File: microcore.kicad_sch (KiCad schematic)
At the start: 7 parts, among them J1 TE_776231-1, J8 USB_B_Mini, M1 Module:mega-mcu100/0.3, M2 Module-power_12and5V-0.3, M3 Module-vr-max9924-0.3

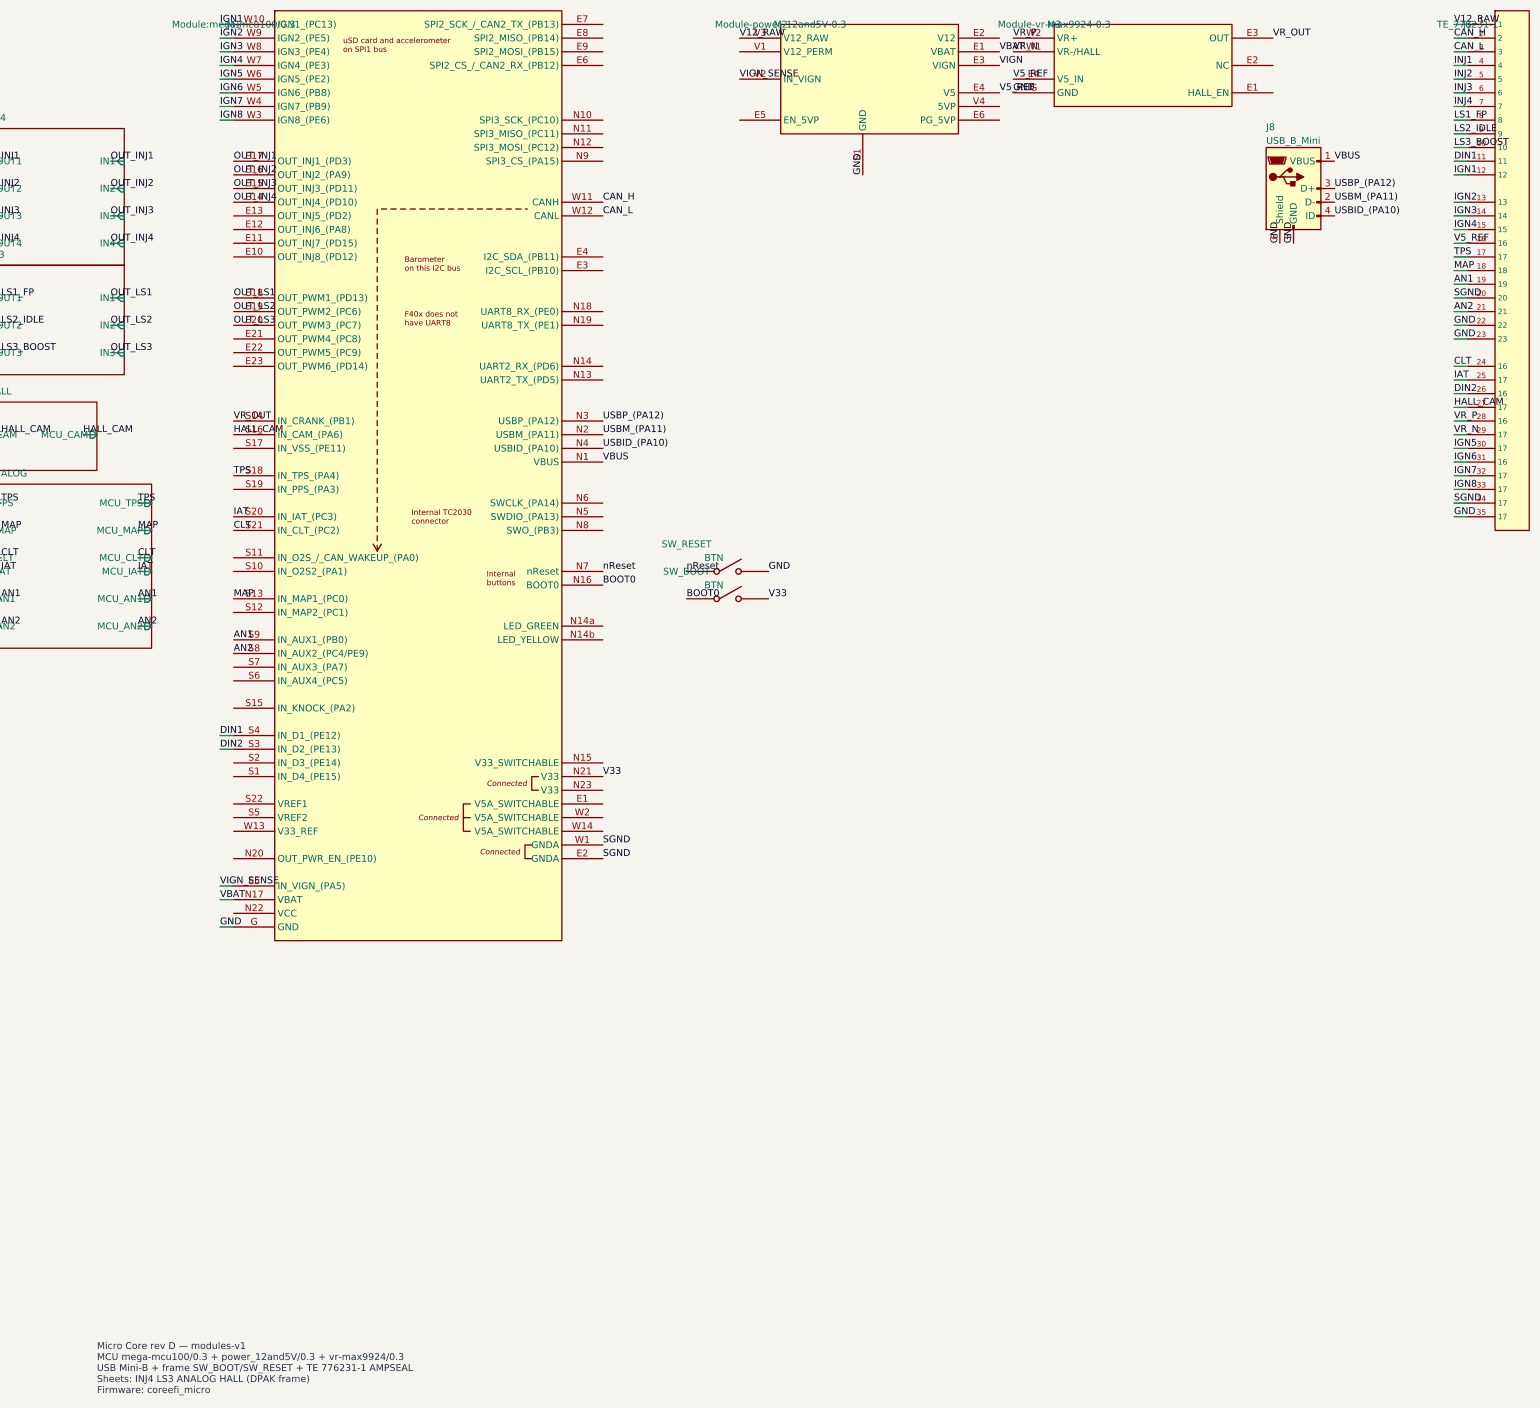
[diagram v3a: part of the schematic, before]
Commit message: Rev e: nest INJ/LS DPAKs on frame, apply netlist, GND pours, route
Place Q1-Q7 + R1-R7 clear of AMPSEAL keepout; unify GND global net;
assign schematic nets to pads; add F/B GND zones and scripted frame
tracks/vias. Module copper remains Create Board gerber merge.
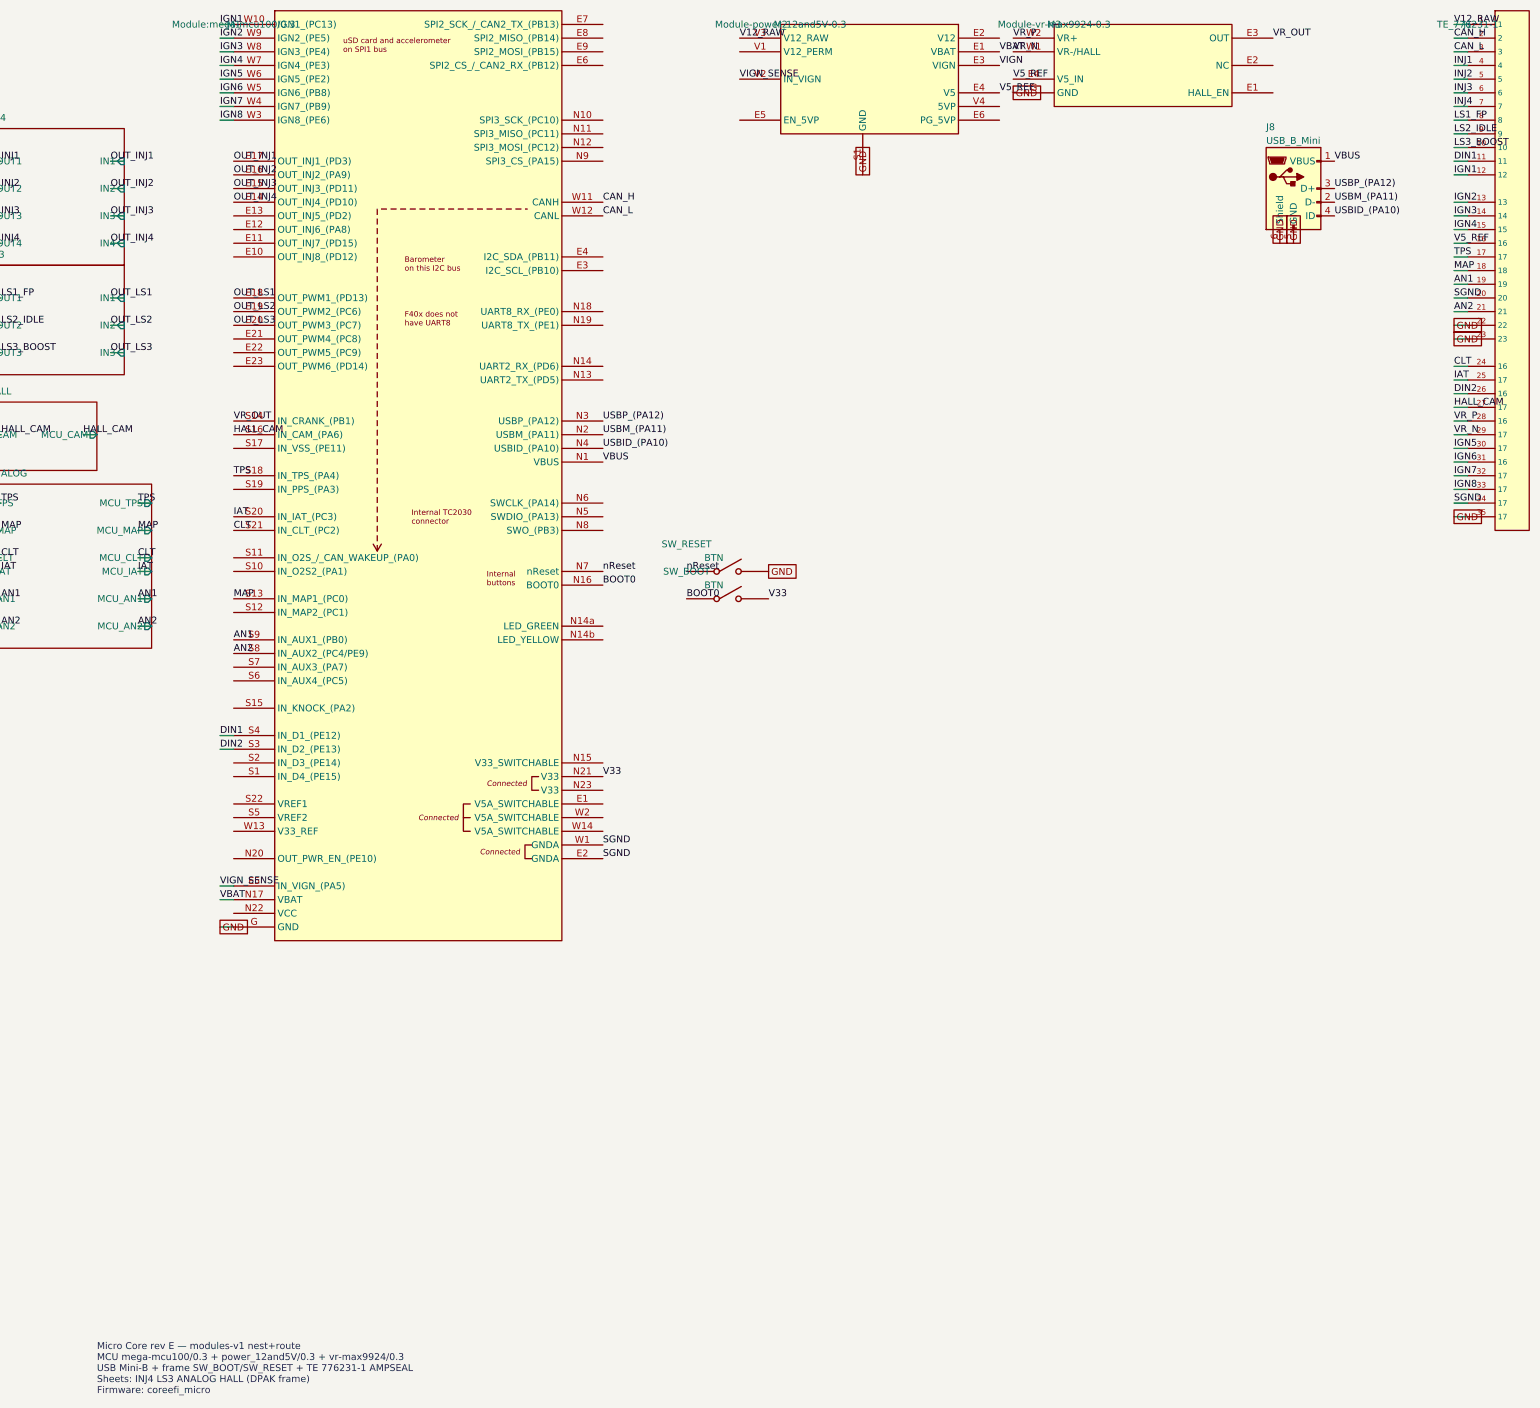
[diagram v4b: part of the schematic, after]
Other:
- note added: "Micro Core rev E — modules-v1 nest+route MCU mega-mcu100/0.3 + power_12and5V/0.3 + vr-max9924/0.3 USB Mini-B + frame SW_BOOT/SW_RESET + TE 776231-1 AMPSEAL Sheets: INJ4 LS3 ANALOG HALL (DPAK frame) Firmware: coreefi_micro"
- note removed: "Micro Core rev D — modules-v1 MCU mega-mcu100/0.3 + power_12and5V/0.3 + vr-max9924/0.3 USB Mini-B + frame SW_BOOT/SW_RESET + TE 776231-1 AMPSEAL Sheets: INJ4 LS3 ANALOG HALL (DPAK frame) Firmware: coreefi_micro"
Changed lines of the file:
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@@
 		(title "Micro Core")
 		(date "2026-09-15")
-		(rev "D")
+		(rev "E")
 		(company "Core EFI")
-		(comment 1 "modules-v1 rev D — pin freeze + frame BOOT/RESET")
+		(comment 1 "modules-v1 rev E — nest DPAKs + frame routing + GND pours")
 		(comment 2 "Firmware board: coreefi_micro")
 		(comment 3 "PCB basename: microcore (no dashes/underscores)")
@@
 		)
 	)
-	(text "Micro Core rev D — modules-v1\nMCU mega-mcu100/0.3 + power_12and5V/0.3 + vr-max9924/0.3\nUSB Mini-B + frame SW_BOOT/SW_RESET + TE 776231-1 AMPSEAL\nSheets: INJ4 LS3 ANALOG HALL (DPAK frame)\nFirmware: coreefi_micro"
+	(text "Micro Core rev E — modules-v1 nest+route\nMCU mega-mcu100/0.3 + power_12and5V/0.3 + vr-max9924/0.3\nUSB Mini-B + frame SW_BOOT/SW_RESET + TE 776231-1 AMPSEAL\nSheets: INJ4 LS3 ANALOG HALL (DPAK frame)\nFirmware: coreefi_micro"
 		(exclude_from_sim no)
 		(at 25.4 280 0)
@@
 		)
 	)
-	(label "GND"
+	(global_label "GND"
 		(at 48.26 193.04 180)
 		(effects
@@
 		)
 	)
-	(label "GND"
+	(global_label "GND"
 		(at 167.64 53.34 90)
 		(effects
@@
 		)
 	)
-	(label "GND"
+	(global_label "GND"
 		(at 277.46 81.28 180)
 		(effects
@@
 		)
 	)
-	(label "GND"
+	(global_label "GND"
 		(at 277.46 83.82 180)
 		(effects
@@
 		)
 	)
-	(label "GND"
+	(global_label "GND"
 		(at 247.65 66.04 90)
 		(effects
@@
 		)
 	)
-	(label "GND"
+	(global_label "GND"
 		(at 245.11 66.04 90)
 		(effects
@@
 		)
 	)
-	(label "GND"
+	(global_label "GND"
 		(at 195.58 38.1 180)
 		(effects
@@
 		)
 	)
-	(label "GND"
+	(global_label "GND"
 		(at 277.46 116.84 180)
 		(effects
@@
 		)
 	)
-	(label "GND"
+	(global_label "GND"
 		(at 150.16 127.0 0)
 		(effects

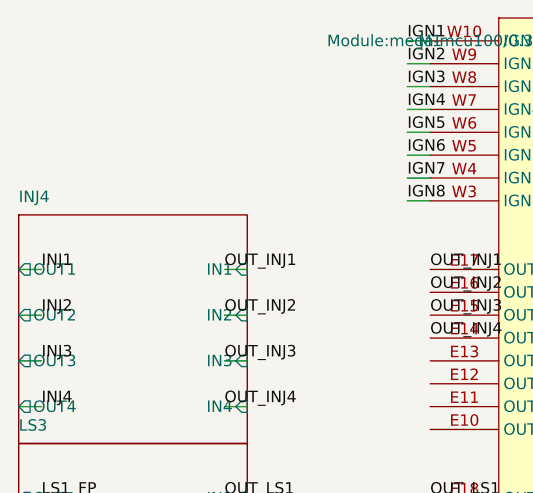
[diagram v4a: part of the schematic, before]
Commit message: Rev j: injector SMAJ33A TVS, US1M flyback, and 2nd 12Ω per INJ channel
SPEC power-stage protection on INJ4 sch+PCB: R8–R11 ballast, D1–D4 US1M,
D5–D8 SMAJ33A (DO-214AC equivalent of SMBJ33A). FET cluster left in place;
new parts in alley + pocket C. BOARD_REVISION bumped to j. PCB remains
substantial (zones + aux origin intact).

Co-authored-by: Quintin <quintinbannink42@users.noreply.github.com>
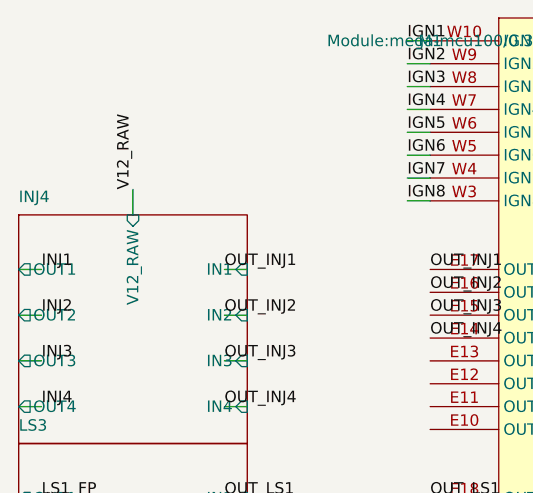
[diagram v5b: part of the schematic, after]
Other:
- sheet INJ4 ports: added V12_RAW; removed none
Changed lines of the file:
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@@
+			)
+		)
+		(pin "V12_RAW" input
+			(at 17.78 44.74 90)
+			(effects
+				(font
+					(size 1.27 1.27)
+				)
+				(justify left)
 			)
 		)
@@
 		)
 	)
+	(wire
+		(pts
+			(xy 17.78 44.74) (xy 17.78 41.91)
+		)
+		(stroke
+			(width 0)
+			(type default)
+		)
+	)
+	(label "V12_RAW"
+		(at 17.78 41.91 90)
+		(effects
+			(font
+				(size 1.27 1.27)
+			)
+			(justify left bottom)
+		)
+	)

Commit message: Rev k: move injector diodes to B.Cu near J1; drop frame buttons
Flip D1-D4 (US1M) and D5-D8 (SMAJ33A) onto the bottom copper on the
west/east flanks of AMPSEAL J1, outside the TE_776231 silk/body keepout,
and delete the old F.Cu alley/pocket-C footprints and 0.4 mm wrap tracks.
Remove frame SW_BOOT/SW_RESET from schematic and PCB (mega-mcu100
internal buttons stay). Bump BOARD_REVISION j to k; PCB stays substantial
with Edge.Cuts drill origin unchanged.

Co-authored-by: Quintin <quintinbannink42@users.noreply.github.com>
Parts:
- removed SW_BOOT, SW_RESET: BTN, hellen-one-common:SMD-2_2.9x3.9x1.7, symbol hellen-one-common:Button_SPST
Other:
- note added: "Micro Core rev E — modules-v1 nest+route MCU mega-mcu100/0.3 + power_12and5V/0.3 + vr-max9924/0.3 USB Mini-B + TE 776231-1 AMPSEAL (frame SW_BOOT/SW_RESET removed rev K) Sheets: INJ4 LS3 ANALOG HALL (DPAK frame) Firmware: coreefi_micro"
- note removed: "Micro Core rev E — modules-v1 nest+route MCU mega-mcu100/0.3 + power_12and5V/0.3 + vr-max9924/0.3 USB Mini-B + frame SW_BOOT/SW_RESET + TE 776231-1 AMPSEAL Sheets: INJ4 LS3 ANALOG HALL (DPAK frame) Firmware: coreefi_micro"
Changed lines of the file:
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@@
 		)
 	)
-	(text "Micro Core rev E — modules-v1 nest+route\nMCU mega-mcu100/0.3 + power_12and5V/0.3 + vr-max9924/0.3\nUSB Mini-B + frame SW_BOOT/SW_RESET + TE 776231-1 AMPSEAL\nSheets: INJ4 LS3 ANALOG HALL (DPAK frame)\nFirmware: coreefi_micro"
+	(text "Micro Core rev E — modules-v1 nest+route\nMCU mega-mcu100/0.3 + power_12and5V/0.3 + vr-max9924/0.3\nUSB Mini-B + TE 776231-1 AMPSEAL (frame SW_BOOT/SW_RESET removed rev K)\nSheets: INJ4 LS3 ANALOG HALL (DPAK frame)\nFirmware: coreefi_micro"
 		(exclude_from_sim no)
 		(at 25.4 280 0)
@@
 		(effects
 			(font
-				(size 1.27 1.27)
-			)
-			(justify left bottom)
-		)
-	)
-	(symbol
-		(lib_id "hellen-one-common:Button_SPST")
-		(at 140 129.54 0)
-		(unit 1)
-		(exclude_from_sim no)
-		(in_bom yes)
-		(on_board yes)
-		(dnp no)
-		(property "Reference" "SW_BOOT"
-			(at 134.92 126.99999999999999 0)
-			(effects
-				(font
-					(size 1.27 1.27)
-				)
-			)
-		)
-		(property "Value" "BTN"
-			(at 140 129.54 0)
-			(effects
-				(font
-					(size 1.27 1.27)
-				)
-			)
-		)
-		(property "Footprint" "hellen-one-common:SMD-2_2.9x3.9x1.7"
-			(at 140 129.54 0)
-			(effects
-				(font
-					(size 1.27 1.27)
-				)
-				(hide yes)
-			)
-		)
-		(property "Datasheet" ""
-			(at 140 129.54 0)
-			(effects
-				(font
-					(size 1.27 1.27)
-				)
-				(hide yes)
-			)
-		)
-		(property "Description" "Frame BOOT0 to V33 (parallels mega S101)"
-			(at 140 129.54 0)
-			(effects
-				(font
-					(size 1.27 1.27)
-				)
-				(hide yes)
-			)
-		)
-		(property "LCSC" "C115357"
-			(at 140 129.54 0)
-			(effects
-				(font
-					(size 1.27 1.27)
-				)
-				(hide yes)
-			)
-		)
-		(pin "1"
-		)
-		(pin "2"
-		)
-		(instances
-			(project "microcore"
-				(path "/a1b2c3d4-e5f6-7890-abcd-ef1234567890"
-					(reference "SW_BOOT")
-					(unit 1)
-				)
-			)
-		)
-	)
-	(symbol
-		(lib_id "hellen-one-common:Button_SPST")
-		(at 140 124.46 0)
-		(unit 1)
-		(exclude_from_sim no)
-		(in_bom yes)
-		(on_board yes)
-		(dnp no)
-		(property "Reference" "SW_RESET"
-			(at 134.92 121.91999999999999 0)
-			(effects
-				(font
-					(size 1.27 1.27)
-				)
-			)
-		)
-		(property "Value" "BTN"
-			(at 140 124.46 0)
-			(effects
-				(font
-					(size 1.27 1.27)
-				)
-			)
-		)
-		(property "Footprint" "hellen-one-common:SMD-2_2.9x3.9x1.7"
-			(at 140 124.46 0)
-			(effects
-				(font
-					(size 1.27 1.27)
-				)
-				(hide yes)
-			)
-		)
-		(property "Datasheet" ""
-			(at 140 124.46 0)
-			(effects
-				(font
-					(size 1.27 1.27)
-				)
-				(hide yes)
-			)
-		)
-		(property "Description" "Frame nReset to GND (parallels mega S100)"
-			(at 140 124.46 0)
-			(effects
-				(font
-					(size 1.27 1.27)
-				)
-				(hide yes)
-			)
-		)
-		(property "LCSC" "C115357"
-			(at 140 124.46 0)
-			(effects
-				(font
-					(size 1.27 1.27)
-				)
-				(hide yes)
-			)
-		)
-		(pin "1"
-		)
-		(pin "2"
-		)
-		(instances
-			(project "microcore"
-				(path "/a1b2c3d4-e5f6-7890-abcd-ef1234567890"
-					(reference "SW_RESET")
-					(unit 1)
-				)
-			)
-		)
-	)
-	(label "BOOT0"
-		(at 134.92 132.08 180)
-		(effects
-			(font
-				(size 1.27 1.27)
-			)
-			(justify left bottom)
-		)
-	)
-	(label "V33"
-		(at 150.16 132.08 0)
-		(effects
-			(font
-				(size 1.27 1.27)
-			)
-			(justify left bottom)
-		)
-	)
-	(label "nReset"
-		(at 134.92 127.0 180)
-		(effects
-			(font
-				(size 1.27 1.27)
-			)
-			(justify left bottom)
-		)
-	)
-	(global_label "GND"
-		(at 150.16 127.0 0)
-		(effects
-			(font
